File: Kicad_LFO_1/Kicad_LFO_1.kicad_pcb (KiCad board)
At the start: 2 copper layers, 100 x 100 mm, 62 parts, among them J101 LFO555, J102 555 Reset, J103 LFO555Charge, J104 Tri, J105 Sine, J201 In1.1, J202 In1.2, J203 In1.3, J204 Out1, J205 In2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

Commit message: Logo - again
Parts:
- added C203: 100n, Capacitor_SMD:C_0805_2012Metric_Pad1.15x1.40mm_HandSolder, B.Cu at (78.5, 92.2)
- added C204: 100n, Capacitor_SMD:C_0805_2012Metric_Pad1.15x1.40mm_HandSolder, B.Cu at (82.0, 92.2)
- added G***: LOGO, AJ:Johansen_engineering_logo_15mm, B.Cu at (80.0, 78.0)
- added G***: LOGO, AJ:Johansen_engineering_logo_15mm, F.Cu at (80.0, 66.5)
- added G***: LOGO, AJ:Johansen_engineering_logo_15mm, B.Cu at (66.5, 57.5)
- added G***: LOGO, AJ:Johansen_engineering_logo_25mm_front_neg5, F.Cu at (66.5, 139.0)
- moved D201 2.00 mm to (83.0, 51.0)
- moved R215 2.00 mm to (79.0, 51.0)
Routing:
- net GND: track 83.5 -> 96.8 mm, vias 8 -> 10
- net Out2: track 48.6 -> 52.0 mm
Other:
- board text added: "MMX2 Johansen Engineering 2019/03/19 - Rev A"

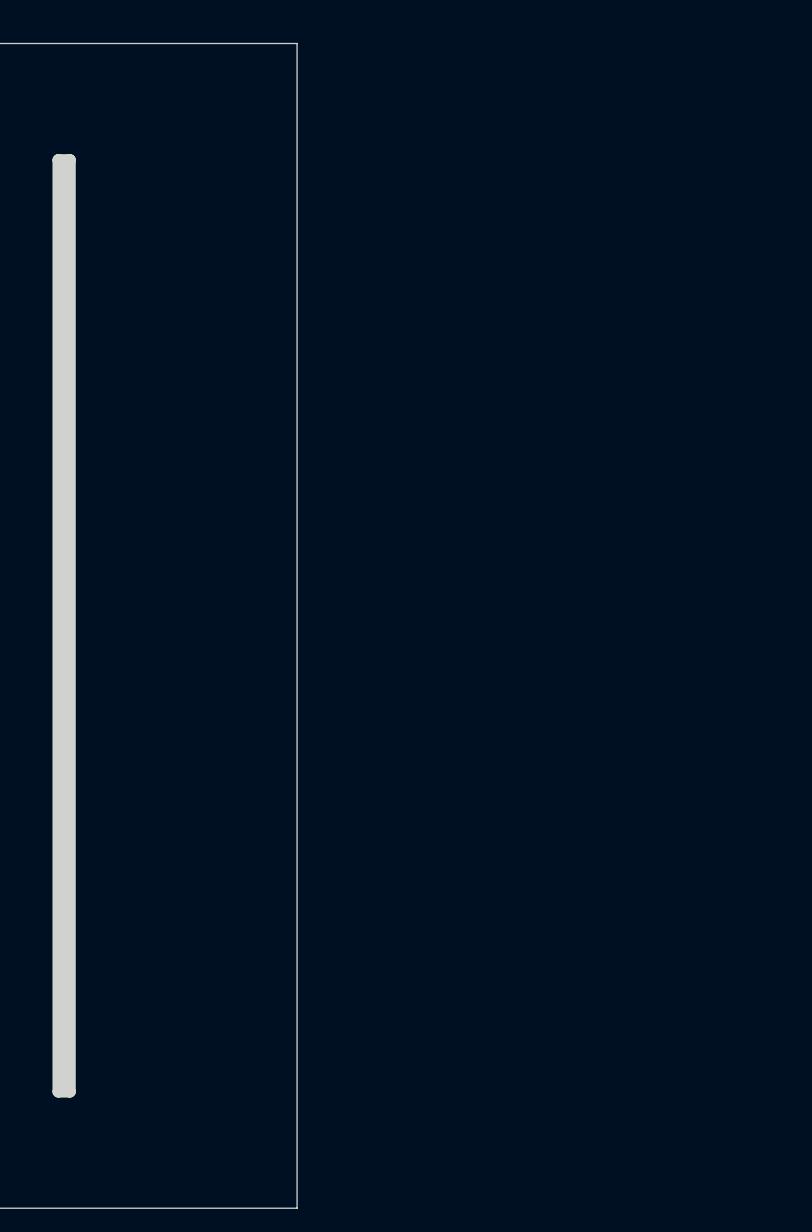
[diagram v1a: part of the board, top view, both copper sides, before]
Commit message: TL072 LFO on PCB
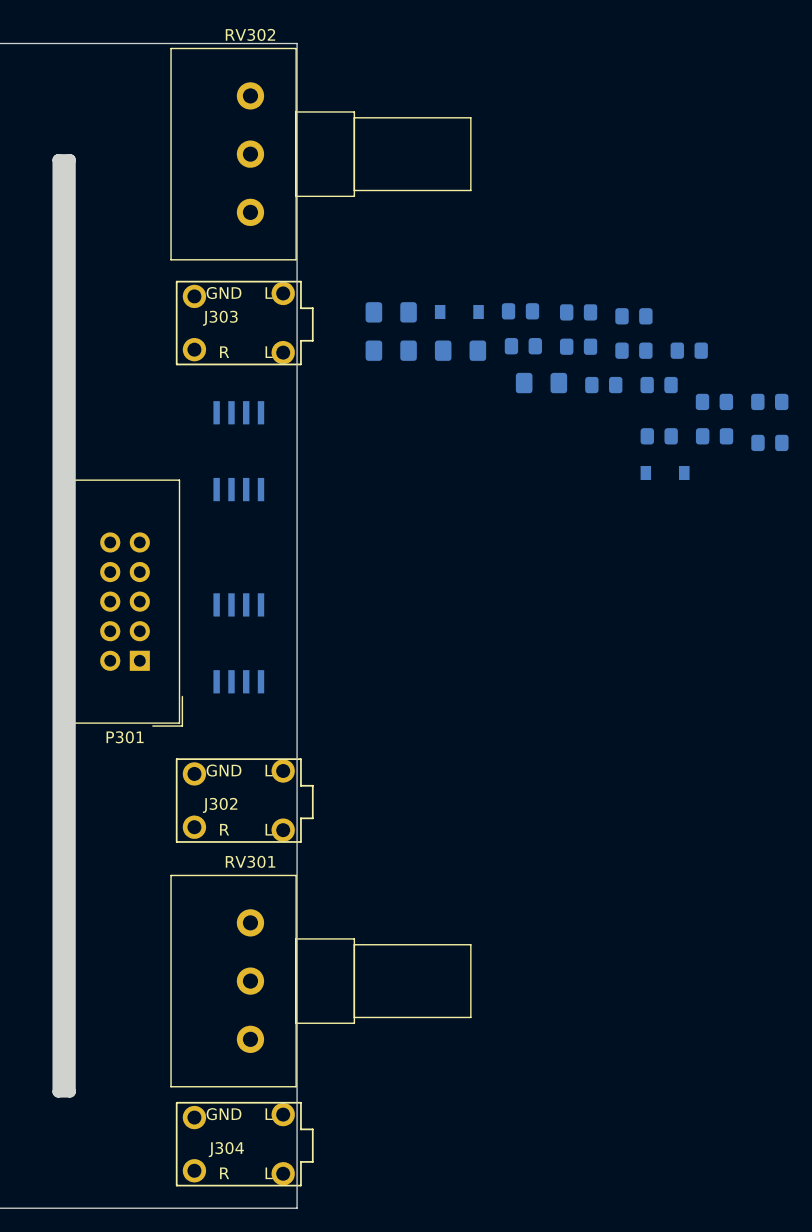
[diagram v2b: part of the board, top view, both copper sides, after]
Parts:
- added C301: 4u7, Capacitor_SMD:C_1206_3216Metric_Pad1.42x1.75mm_HandSolder, B.Cu at (158.1, 73.1)
- added C302: 4u7, Capacitor_SMD:C_1206_3216Metric_Pad1.42x1.75mm_HandSolder, B.Cu at (171.0, 79.2)
- added C303: 470n, Capacitor_SMD:C_0805_2012Metric_Pad1.15x1.40mm_HandSolder, B.Cu at (183.7, 76.4)
- added C304: 100n, Capacitor_SMD:C_1206_3216Metric_Pad1.42x1.75mm_HandSolder, B.Cu at (158.1, 76.4)
- added C305: 100n, Capacitor_SMD:C_1206_3216Metric_Pad1.42x1.75mm_HandSolder, B.Cu at (164.0, 76.4)
- added D301: LED, LED_SMD:LED_0805_2012Metric_Pad1.15x1.40mm_HandSolder, B.Cu at (169.4, 76.0)
- added D302: 1N4148W, Diode_SMD:D_SOD-123, B.Cu at (181.6, 86.9)
- added D303: 1N4148W, Diode_SMD:D_SOD-123, B.Cu at (163.9, 73.1)
- added J302: Tri, AJ-Dropbox-Kicad:AudioJack3StereoNarrow-PJ-321, F.Cu at (145.0, 115.0)
- added J303: LFO_SQ, AJ-Dropbox-Kicad:AudioJack3StereoNarrow-PJ-321, F.Cu at (145.0, 74.0)
- added J304: Sine, AJ-Dropbox-Kicad:AudioJack3StereoNarrow-PJ-321, F.Cu at (145.0, 144.5)
- added P301: HEADER_2x5_Doepfer, Connector_IDC:IDC-Header_2x05_P2.54mm_Vertical, F.Cu at (136.5, 103.0)
- added R301: 1k, Resistor_SMD:R_0805_2012Metric_Pad1.15x1.40mm_HandSolder, B.Cu at (181.1, 79.3)
- added R302: 10k, Resistor_SMD:R_0805_2012Metric_Pad1.15x1.40mm_HandSolder, B.Cu at (174.2, 76.0)
- added R303: 22k, Resistor_SMD:R_0805_2012Metric_Pad1.15x1.40mm_HandSolder, B.Cu at (190.6, 80.8)
- added R304: 1k, Resistor_SMD:R_0805_2012Metric_Pad1.15x1.40mm_HandSolder, B.Cu at (169.2, 73.0)
- added R305: 10k, Resistor_SMD:R_0805_2012Metric_Pad1.15x1.40mm_HandSolder, B.Cu at (176.3, 79.3)
- added R306: 10k, Resistor_SMD:R_0805_2012Metric_Pad1.15x1.40mm_HandSolder, B.Cu at (181.1, 83.7)
- added R307: 1k, Resistor_SMD:R_0805_2012Metric_Pad1.15x1.40mm_HandSolder, B.Cu at (174.2, 73.1)
- added R308: 10k, Resistor_SMD:R_0805_2012Metric_Pad1.15x1.40mm_HandSolder, B.Cu at (185.8, 83.7)
- added R309: 33k, Resistor_SMD:R_0805_2012Metric_Pad1.15x1.40mm_HandSolder, B.Cu at (178.9, 76.4)
- added R310: 1k, Resistor_SMD:R_0805_2012Metric_Pad1.15x1.40mm_HandSolder, B.Cu at (185.8, 80.8)
- added R311: 100k, Resistor_SMD:R_0805_2012Metric_Pad1.15x1.40mm_HandSolder, B.Cu at (178.9, 73.4)
- added R312: 390k, Resistor_SMD:R_0805_2012Metric_Pad1.15x1.40mm_HandSolder, B.Cu at (190.6, 84.3)
- added RV301: 10k Sine, Potentiometer_THT:Potentiometer_Alps_RK163_Single_Horizontal, F.Cu at (146.0, 135.5)
- added RV302: 100k Freq, Potentiometer_THT:Potentiometer_Alps_RK163_Single_Horizontal, F.Cu at (146.0, 64.5)
- added U301: TL072, AJ-Dropbox-Kicad:AJ_SO-8_5.3x6.2mm_P1.27mm, B.Cu at (145.0, 101.5)
- added U302: TL072, AJ-Dropbox-Kicad:AJ_SO-8_5.3x6.2mm_P1.27mm, B.Cu at (145.0, 85.0)

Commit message: Update Kicad_LFO_1.kicad_pcb
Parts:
- added C401: 4u7, Capacitor_SMD:C_1206_3216Metric_Pad1.42x1.75mm_HandSolder, B.Cu at (94.2, 56.8)
- added C402: 4u7, Capacitor_SMD:C_1206_3216Metric_Pad1.42x1.75mm_HandSolder, B.Cu at (94.2, 63.8)
- added D401: LED, LED_SMD:LED_0805_2012Metric_Pad1.15x1.40mm_HandSolder, B.Cu at (107.0, 54.0)
- added D402: MRA4007T3G, Diode_SMD:D_SOD-123, B.Cu at (96.8, 101.8)
- added D403: MRA4007T3G, Diode_SMD:D_SOD-123, B.Cu at (101.8, 101.8)
- added D404: MRA4007T3G, Diode_SMD:D_SOD-123, B.Cu at (96.8, 111.0)
- added D405: MRA4007T3G, Diode_SMD:D_SOD-123, B.Cu at (101.9, 111.0)
- added D406: MRA4007T3G, Diode_SMD:D_SOD-123, B.Cu at (96.8, 141.5)
- added D407: MRA4007T3G, Diode_SMD:D_SOD-123, B.Cu at (101.8, 141.5)
- added D408: MRA4007T3G, Diode_SMD:D_SOD-123, B.Cu at (96.8, 132.5)
- added D409: MRA4007T3G, Diode_SMD:D_SOD-123, B.Cu at (101.9, 132.5)
- added D410: MRA4007T3G, Diode_SMD:D_SOD-123, B.Cu at (96.8, 75.5)
- added D411: MRA4007T3G, Diode_SMD:D_SOD-123, B.Cu at (101.8, 75.5)
- added J401: NAND_IN1, AJ-Dropbox-Kicad:PJ301SM, F.Cu at (100.0, 105.0)
- added J402: NAND_OUT, AJ-Dropbox-Kicad:PJ301SM, F.Cu at (100.0, 94.5)
- added J403: NAND_IN2, AJ-Dropbox-Kicad:PJ301SM, F.Cu at (100.0, 114.0)
- added J404: AND_IN1, AJ-Dropbox-Kicad:PJ301SM, F.Cu at (100.0, 145.0)
- added J405: AND_OUT, AJ-Dropbox-Kicad:PJ301SM, F.Cu at (100.0, 125.5)
- added J406: AND_IN2, AJ-Dropbox-Kicad:PJ301SM, F.Cu at (100.0, 135.9)
- added J407: NOT_OUT, AJ-Dropbox-Kicad:PJ301SM, F.Cu at (100.0, 70.8)
- added J408: NOT_IN, AJ-Dropbox-Kicad:PJ301SM, F.Cu at (100.0, 80.2)
- added P401: HEADER_2x5_Doepfer, Connector_IDC:IDC-Header_2x05_P2.54mm_Vertical, B.Cu at (99.0, 65.5)
- added R401: 22k, Resistor_SMD:R_0805_2012Metric_Pad1.15x1.40mm_HandSolder, B.Cu at (107.0, 51.8)
- added U402: 74LS00, Package_SO:SOIC-14_3.9x8.7mm_P1.27mm, B.Cu at (99.8, 87.2)
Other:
- outline, holes or cut-outs redrawn

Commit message: U401 remove
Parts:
- added U401: TL072, AJ-Dropbox-Kicad:AJ_SO-8_5.3x6.2mm_P1.27mm, F.Cu at (101.0, 34.8)
- moved R401 15.7 mm to (92.2, 57.0), turned to 90 degrees
- moved D401 15.1 mm to (92.0, 52.2), turned to 90 degrees
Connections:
- U402 pad 7: -12V -> GND
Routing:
- net +12V: track 99.7 -> 257.5 mm, vias 1 -> 3
- net AND_IN1: track 0.00 -> 63.9 mm
- net AND_IN2: track 0.00 -> 57.5 mm
- net GND: track 96.8 -> 147.2 mm, vias 10 -> 11
- net Net-(J405-PadT): track 0.00 -> 43.8 mm, vias 0 -> 2
- net NAND_IN2: track 0.00 -> 30.1 mm
- net -12V: track 43.7 -> 64.8 mm
- net NAND_IN1: track 0.00 -> 18.3 mm
- net NOT_IN: track 0.00 -> 17.9 mm
- net Net-(J407-PadT): track 0.00 -> 16.9 mm
- net Net-(U402-Pad12): track 0.00 -> 11.1 mm
- net Net-(J402-PadT): track 0.00 -> 7.06 mm
- net Net-(D401-Pad2): track 0.00 -> 5.52 mm

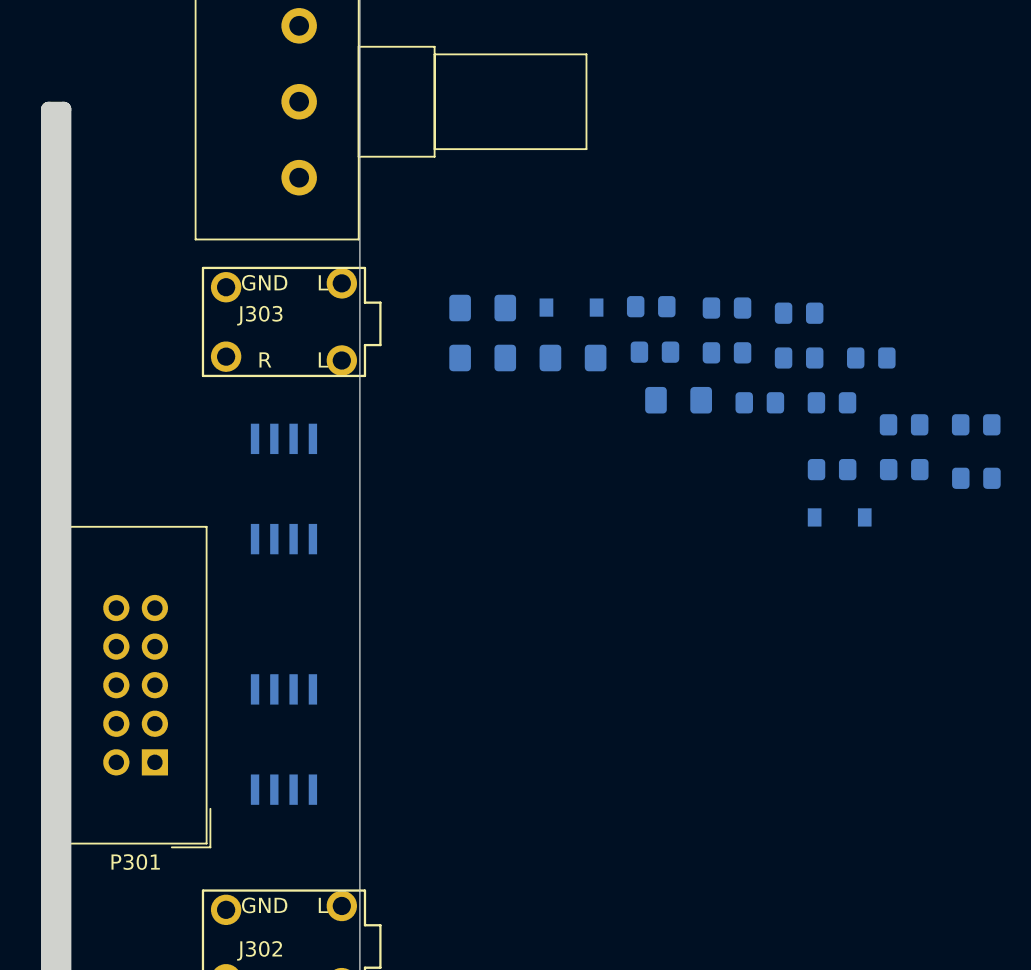
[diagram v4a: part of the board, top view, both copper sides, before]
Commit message: OpAmp LFO components placed
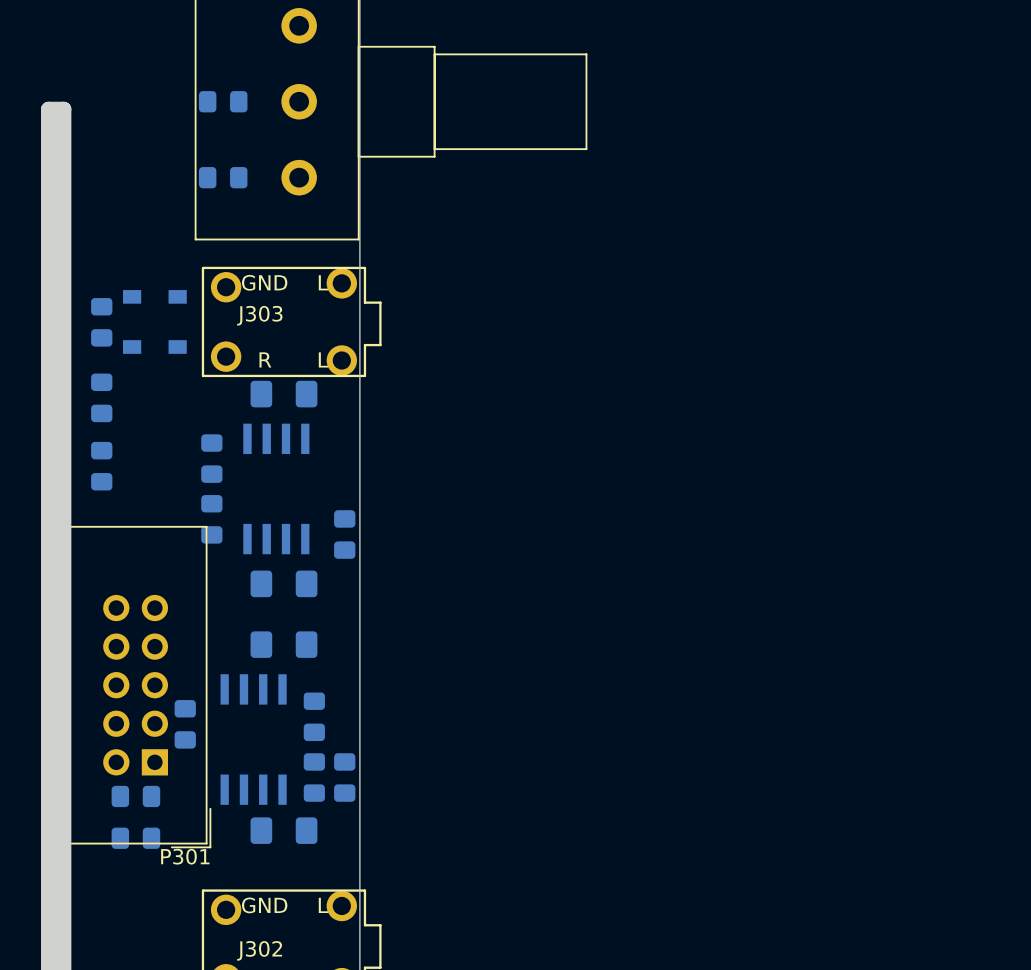
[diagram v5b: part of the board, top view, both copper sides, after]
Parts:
- moved R303 61.7 mm to (135.2, 108.0)
- moved R312 55.4 mm to (141.0, 59.5), turned to 180 degrees
- moved D302 48.3 mm to (135.0, 74.0), turned to 90 degrees
- moved R306 48.1 mm to (133.0, 83.5), turned to 90 degrees
- moved R310 47.7 mm to (141.0, 64.5), turned to 180 degrees
- moved R301 47.6 mm to (138.5, 100.5), turned to 270 degrees
- moved R308 45.7 mm to (140.2, 87.0), turned to 90 degrees
- moved D301 45.0 mm to (135.2, 105.2)
- moved C303 44.3 mm to (149.0, 104.0), turned to 90 degrees
- moved R311 44.2 mm to (147.0, 104.0), turned to 270 degrees
- moved R305 43.7 mm to (133.0, 74.0), turned to 270 degrees
- moved R309 39.2 mm to (140.2, 83.0), turned to 90 degrees
- moved C302 38.5 mm to (145.0, 107.5)
- moved R304 36.7 mm to (133.0, 79.0), turned to 270 degrees
- moved R302 36.2 mm to (147.0, 100.0), turned to 90 degrees
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
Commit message: Update Kicad_LFO_1.kicad_pcb
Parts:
- moved R307 1.50 mm to (149.0, 89.5)
- moved C305 0.25 mm to (145.0, 91.5)
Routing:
- net Net-(D302-Pad1): track 0.00 -> 75.3 mm
- net Sine3: track 0.00 -> 61.0 mm
- net Tri3: track 0.00 -> 58.6 mm, vias 0 -> 2
- net GND: track 147.2 -> 204.6 mm, vias 11 -> 16
- net Net-(C303-Pad2): track 0.00 -> 54.5 mm, vias 0 -> 4
- net Net-(R309-Pad2): track 0.00 -> 53.5 mm
- net -12V: track 64.8 -> 106.5 mm
- net +12V: track 257.5 -> 292.7 mm, vias 3 -> 5
- net Net-(R304-Pad2): track 0.00 -> 21.5 mm, vias 0 -> 2
- net Square3: track 0.00 -> 14.2 mm
- net Net-(R301-Pad2): track 0.00 -> 12.1 mm
- net Net-(R307-Pad2): track 0.00 -> 7.41 mm
- net Net-(R308-Pad2): track 0.00 -> 7.37 mm
- net Square3fb: track 0.00 -> 3.97 mm
- net Net-(R310-Pad1): track 0.00 -> 3.97 mm
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
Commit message: Update Kicad_LFO_1.kicad_pcb
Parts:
- removed U401: TL072, AJ-Dropbox-Kicad:AJ_SO-8_5.3x6.2mm_P1.27mm
- added G***: LOGO, AJ:Johansen_engineering_logo_15mm, B.Cu at (134.0, 57.0)
- added G***: LOGO, AJ:Johansen_engineering_logo_15mm, B.Cu at (107.0, 57.5)
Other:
- board text added: "LFO1 Johansen Engineering 2019/04/15 - Rev A"

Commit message: THT Placed
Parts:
- added C501: 4u7, Capacitor_SMD:C_1206_3216Metric_Pad1.42x1.75mm_HandSolder, B.Cu at (119.7, 22.9)
- added C502: 4u7, Capacitor_SMD:C_1206_3216Metric_Pad1.42x1.75mm_HandSolder, B.Cu at (119.7, 19.6)
- added D501: LED, LED_SMD:LED_0805_2012Metric_Pad1.15x1.40mm_HandSolder, B.Cu at (130.1, 36.1)
- added D502: MRA4007T3G, Diode_SMD:D_SOD-123, B.Cu at (124.8, 36.0)
- added D503: MRA4007T3G, Diode_SMD:D_SOD-123, B.Cu at (130.6, 39.3)
- added D504: MRA4007T3G, Diode_SMD:D_SOD-123, B.Cu at (124.8, 39.3)
- added J501: FF_In1, AJ-Dropbox-Kicad:PJ301SM, F.Cu at (120.0, 81.5)
- added J502: FF_In2, AJ-Dropbox-Kicad:PJ301SM, F.Cu at (120.0, 125.2)
- added J503: FF_Out1, AJ-Dropbox-Kicad:PJ301SM, F.Cu at (120.0, 95.5)
- added J504: FF_Out2, AJ-Dropbox-Kicad:PJ301SM, F.Cu at (120.0, 139.2)
- added P501: HEADER_2x5_Doepfer, Connector_IDC:IDC-Header_2x05_P2.54mm_Vertical, B.Cu at (118.8, 65.5)
- added R501: 22k, Resistor_SMD:R_0805_2012Metric_Pad1.15x1.40mm_HandSolder, B.Cu at (125.1, 23.0)
- added R502: 4k7, Resistor_SMD:R_0805_2012Metric_Pad1.15x1.40mm_HandSolder, B.Cu at (125.1, 20.1)
- added R503: 4k7, Resistor_SMD:R_0805_2012Metric_Pad1.15x1.40mm_HandSolder, B.Cu at (124.3, 32.8)
- added R504: 4k7, Resistor_SMD:R_0805_2012Metric_Pad1.15x1.40mm_HandSolder, B.Cu at (124.3, 29.9)
- added R505: 4k7, Resistor_SMD:R_0805_2012Metric_Pad1.15x1.40mm_HandSolder, B.Cu at (115.9, 29.2)
- added U501: 4013, Package_SO:SOIC-14_3.9x8.7mm_P1.27mm, B.Cu at (117.7, 35.8)
